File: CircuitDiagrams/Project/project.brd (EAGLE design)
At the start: 100 x 70 mm, 124 parts, among them IC1 UC3C, IC2 PCA9542A, IC3 MT48LC4M16A2TSOP54, IC4 TB6593FNGSSOP20, IC5 TB6593FNGSSOP20, J1 JTAG2.54MM2X5TH, J2 1BY2THROUGHHOLE, J3 1BY2THROUGHHOLE, J4 1BY2THROUGHHOLE, J5 8PIN2.54MM2X4TH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

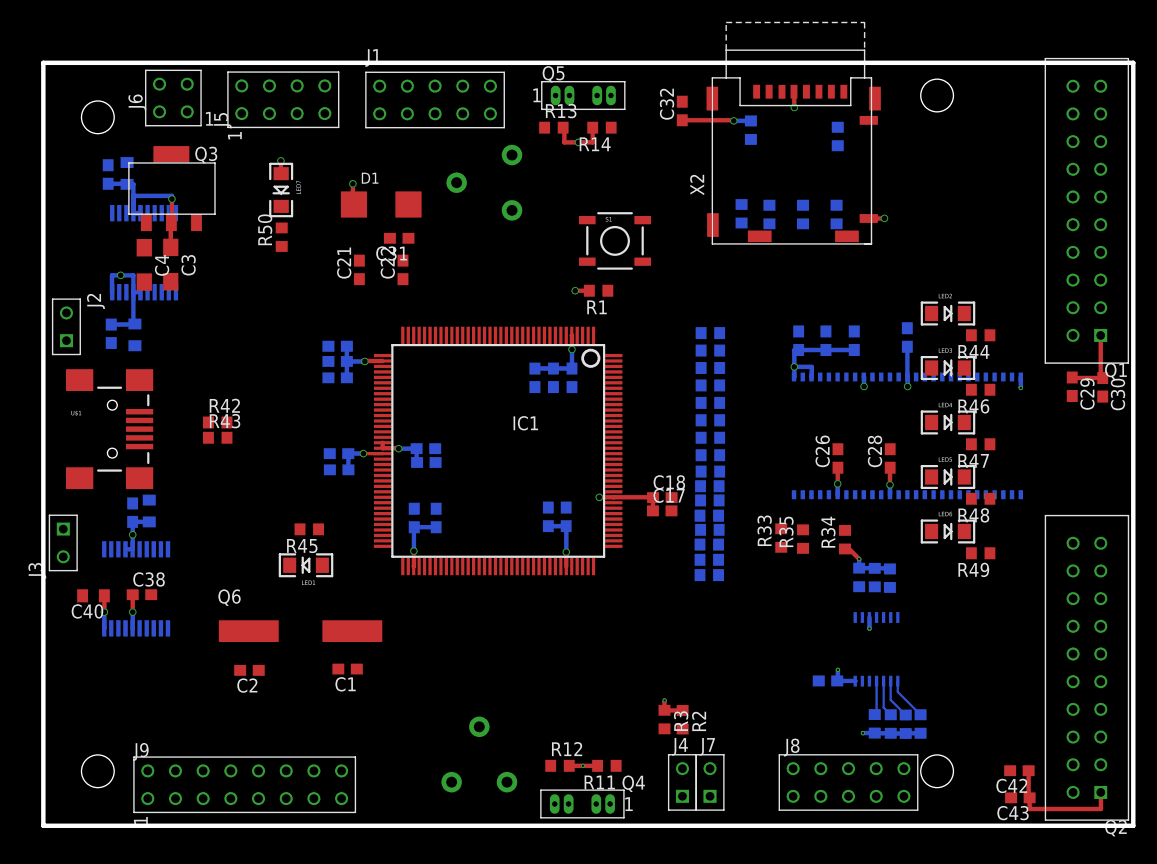
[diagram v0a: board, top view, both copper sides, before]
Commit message: Half way through routing the GND Connections
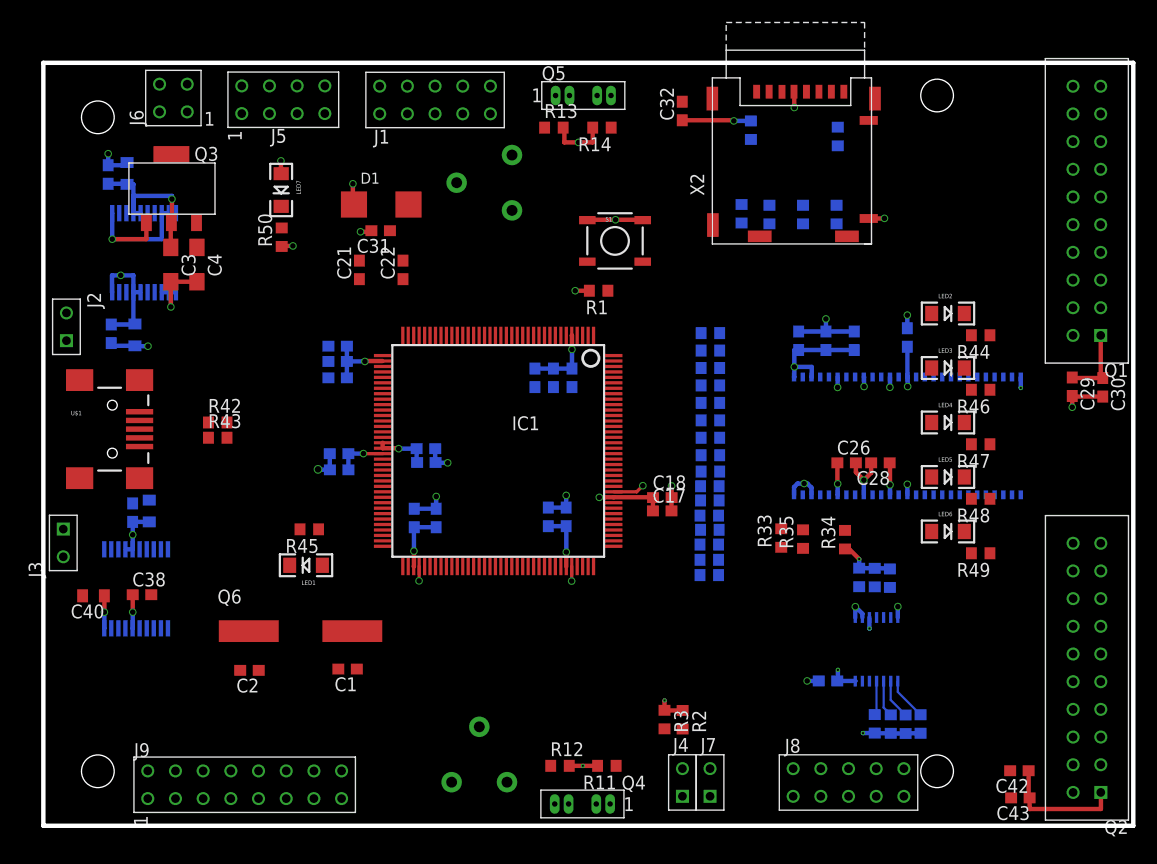
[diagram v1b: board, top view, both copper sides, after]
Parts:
- moved C4 4.83 mm to (14.1, 51.5)
- moved C31 1.84 mm to (30.9, 54.6)
- moved C28 0.98 mm to (76.8, 33.3), turned to 180 degrees
- moved C26 0.89 mm to (73.7, 33.3), turned to 0 degrees
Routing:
- net GND: track 0.00 -> 83.5 mm, vias 0 -> 26

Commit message: Finished Wiring GND. Done USB Data and oscillator
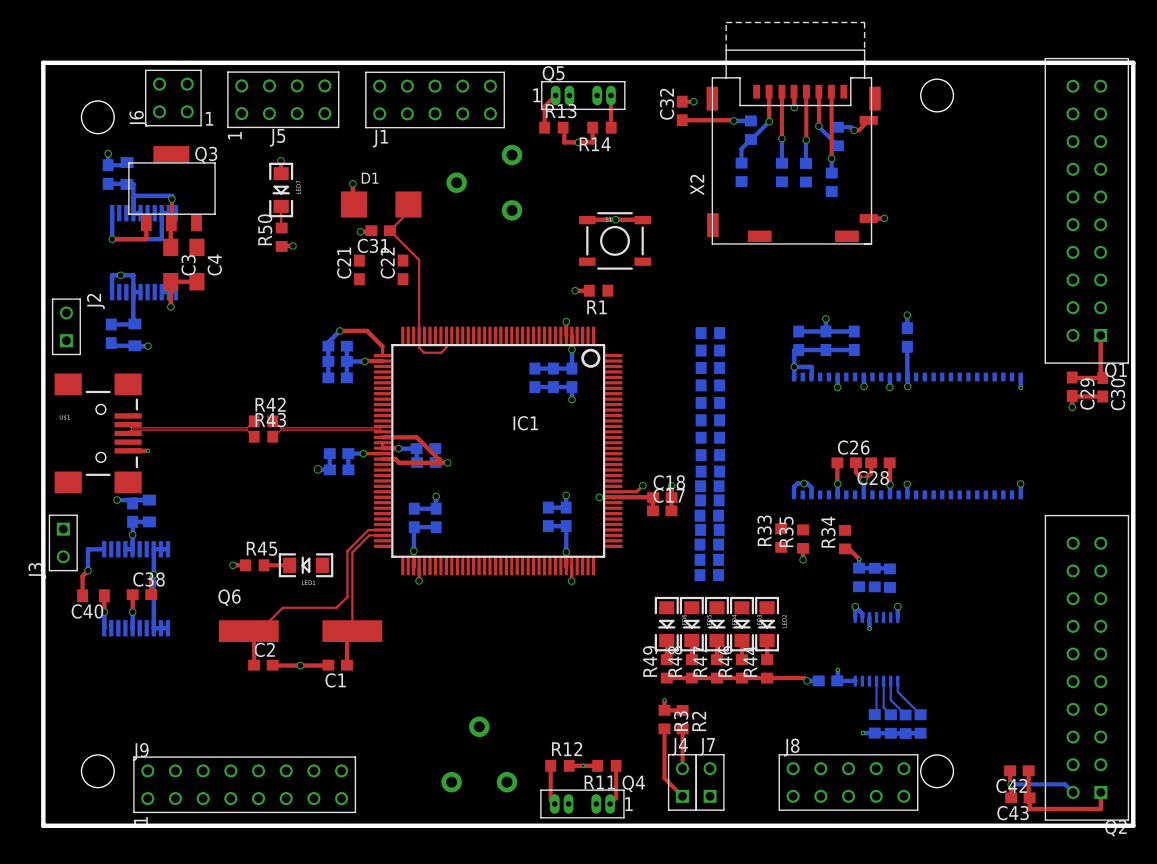
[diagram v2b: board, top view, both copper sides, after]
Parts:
- moved R44 36.3 mm to (66.4, 14.4), turned to 90 degrees
- moved R46 33.7 mm to (64.1, 14.4), turned to 90 degrees
- moved LED2 33.0 mm to (66.4, 18.5), turned to 270 degrees
- moved R47 31.8 mm to (61.8, 14.4), turned to 90 degrees
- moved R48 30.8 mm to (59.5, 14.4), turned to 90 degrees
- moved R49 30.7 mm to (57.2, 14.4), turned to 90 degrees
- moved LED3 30.2 mm to (64.1, 18.5), turned to 270 degrees
- moved LED4 28.1 mm to (61.8, 18.5), turned to 270 degrees
- moved LED6 27.2 mm to (57.2, 18.5), turned to 270 degrees
- moved LED5 27.1 mm to (59.5, 18.5), turned to 270 degrees
- moved R45 5.99 mm to (19.4, 23.9), turned to 0 degrees
- moved R42 4.20 mm to (20.2, 37.1)
- moved R43 4.20 mm to (20.2, 35.7)
- moved R38 4.02 mm to (67.8, 59.9)
- moved R39 3.85 mm to (70.0, 59.9)
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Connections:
- net N$28 renamed DATA_N
- net N$29 renamed DATA_P
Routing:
- net GND: track 83.5 -> 173.3 mm, vias 26 -> 40
- net PB30: track 0.00 -> 21.6 mm
- net PA16: track 0.00 -> 19.0 mm
- net PB31: track 0.00 -> 14.0 mm
- net USB_N: track 0.00 -> 11.9 mm
- net USB_P: track 0.00 -> 11.9 mm
- net DATA_P: track 0.00 -> 10.4 mm
- net DATA_N: track 0.00 -> 10.4 mm
- net N$23: track 0.00 -> 7.64 mm, vias 0 -> 1
- net N$27: track 0.00 -> 7.48 mm, vias 0 -> 1
- net PC2: track 0.00 -> 6.87 mm
- net N$26: track 0.00 -> 6.60 mm, vias 0 -> 1
- net N$25: track 0.00 -> 6.56 mm, vias 0 -> 1
- net N$5: track 0.00 -> 3.73 mm
- net PA6: track 0.00 -> 3.65 mm
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
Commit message: Routed DQ Lines on the SDRAM.
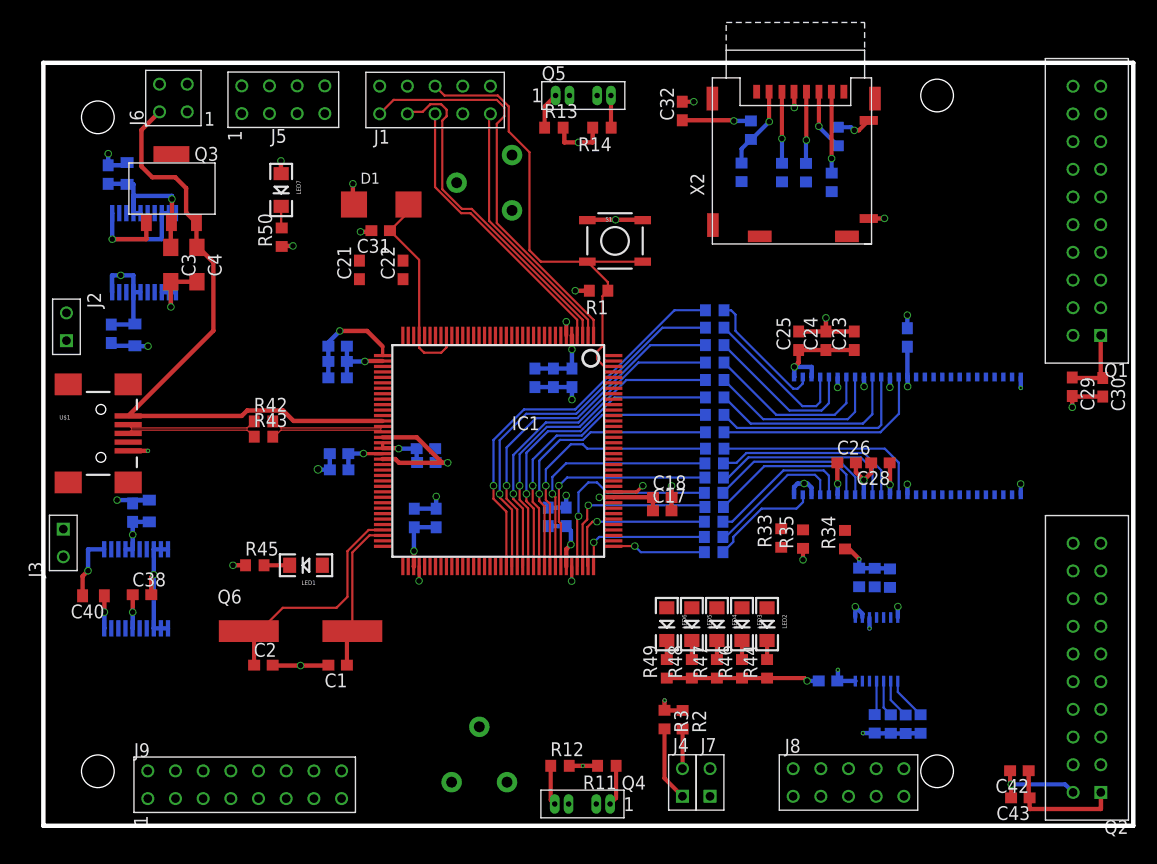
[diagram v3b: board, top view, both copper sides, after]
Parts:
- moved R18 2.14 mm to (61.6, 45.7)
- moved R19 2.14 mm to (61.6, 44.1)
- moved R20 2.14 mm to (61.6, 42.5)
- moved R21 2.14 mm to (61.6, 40.9)
- moved R23 2.14 mm to (61.6, 37.7)
- moved R24 2.14 mm to (61.6, 36.1)
- moved R25 2.14 mm to (61.6, 34.6)
- moved R26 2.14 mm to (61.5, 33.2)
- moved R28 2.14 mm to (61.5, 30.6)
- moved R29 2.14 mm to (61.5, 29.2)
- moved R31 2.14 mm to (61.5, 26.5)
- moved R32 2.14 mm to (61.5, 25.1)
- moved R27 2.14 mm to (61.5, 31.9)
- moved R30 2.14 mm to (61.5, 27.9)
- moved R17 2.14 mm to (61.6, 47.3)
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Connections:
- net N$10 renamed DQ03
- net N$11 renamed DQ04
- net N$12 renamed DQ05
- net N$13 renamed DQ06
- net N$14 renamed DQ07
- net N$15 renamed DQ08
- net N$16 renamed DQ09
- net N$17 renamed DQ10
- net N$18 renamed DQ11
- net N$19 renamed DQ12
- net N$20 renamed DQ13
- net N$21 renamed DQ14
- net N$22 renamed DQ15
- net N$7 renamed DQ00
- net N$8 renamed DQ01
- net N$9 renamed DQ02
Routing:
- net +5V: track 0.00 -> 59.8 mm
- net RESET_N: track 0.00 -> 44.3 mm
- net PA0: track 0.00 -> 37.1 mm
- net PC19: track 0.00 -> 36.5 mm, vias 0 -> 1
- net PC20: track 0.00 -> 35.2 mm, vias 0 -> 1
- net PC21: track 0.00 -> 33.5 mm, vias 0 -> 1
- net PC22: track 0.00 -> 31.7 mm, vias 0 -> 1
- net PA2: track 0.00 -> 30.9 mm
- net PC23: track 0.00 -> 30.5 mm, vias 0 -> 1
- net PC24: track 0.00 -> 29.3 mm, vias 0 -> 1
- net PC25: track 0.00 -> 27.6 mm, vias 0 -> 1
- net PC26: track 0.00 -> 26.2 mm, vias 0 -> 1
- net PA3: track 0.00 -> 26.2 mm
- net PC27: track 0.00 -> 24.8 mm, vias 0 -> 1
- net PA1: track 0.00 -> 24.1 mm
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
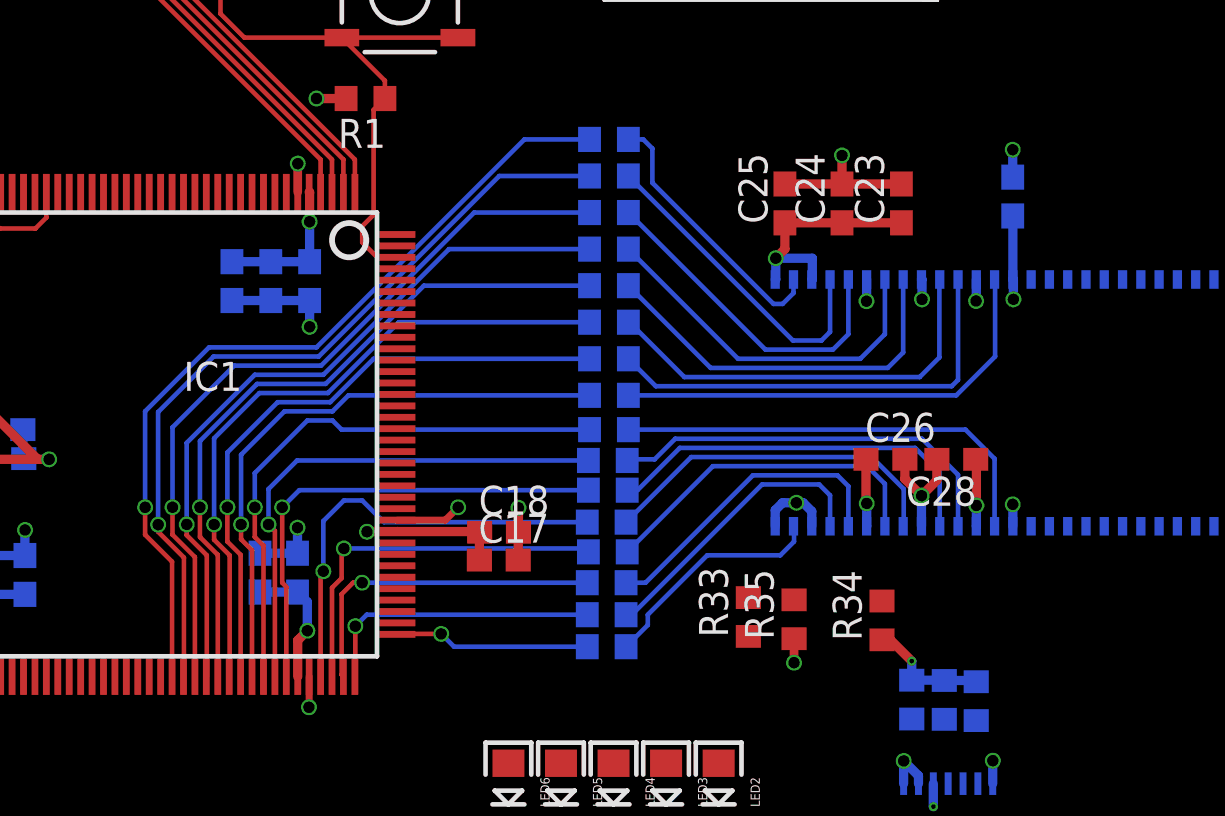
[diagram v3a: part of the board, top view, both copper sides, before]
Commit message: Ripped up SDRAM lines due to poor routing. Working on it again
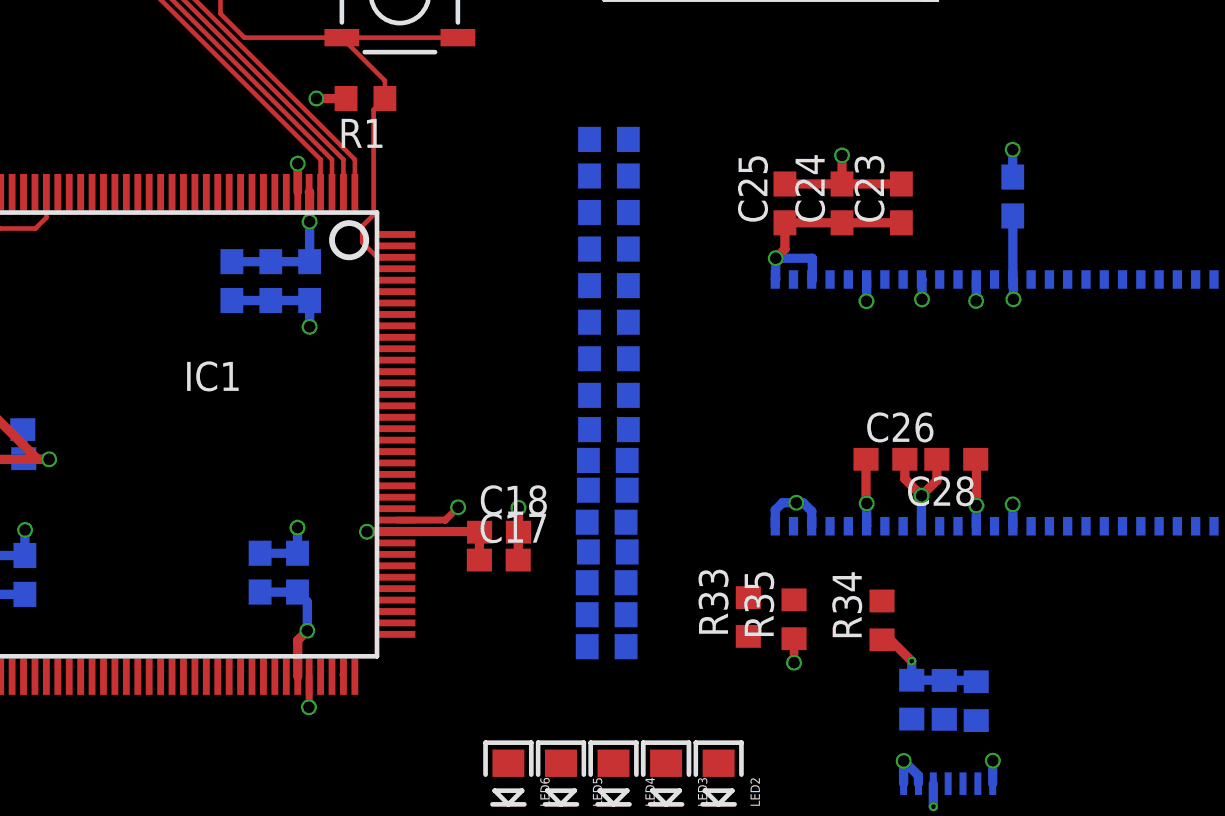
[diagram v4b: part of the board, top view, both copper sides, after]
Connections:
- net N$24 renamed SDRAMCLK
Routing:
- net PC19: track 36.5 -> 0.00 mm, vias 1 -> 0
- net PC20: track 35.2 -> 0.00 mm, vias 1 -> 0
- net PC21: track 33.5 -> 0.00 mm, vias 1 -> 0
- net PC22: track 31.7 -> 0.00 mm, vias 1 -> 0
- net PC23: track 30.5 -> 0.00 mm, vias 1 -> 0
- net PC24: track 29.3 -> 0.00 mm, vias 1 -> 0
- net PC25: track 27.6 -> 0.00 mm, vias 1 -> 0
- net PC26: track 26.2 -> 0.00 mm, vias 1 -> 0
- net PC27: track 24.8 -> 0.00 mm, vias 1 -> 0
- net PC28: track 22.8 -> 0.00 mm, vias 1 -> 0
- net PC29: track 21.2 -> 0.00 mm, vias 1 -> 0
- net DQ07: track 20.1 -> 0.03 mm
- net DQ08: track 19.5 -> 0.00 mm
- net DQ06: track 19.4 -> 0.00 mm
- net PC30: track 19.2 -> 0.00 mm, vias 1 -> 0
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
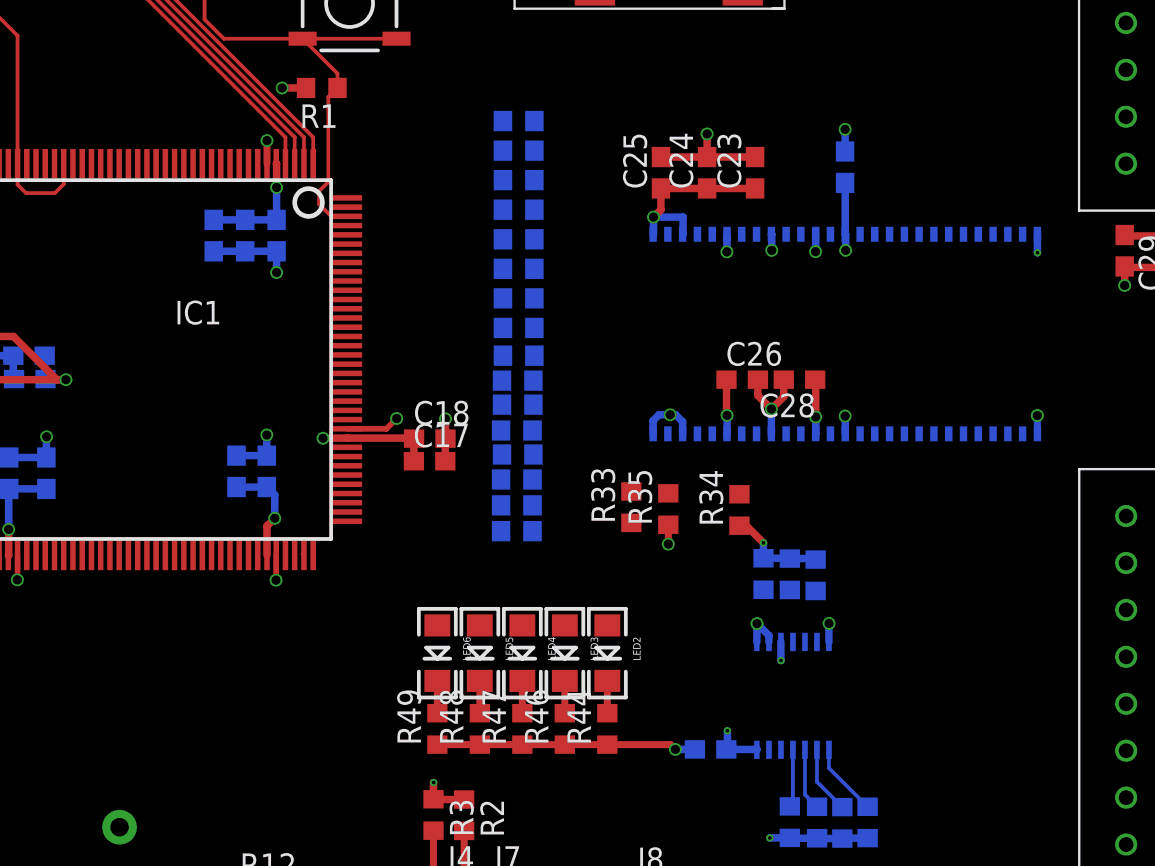
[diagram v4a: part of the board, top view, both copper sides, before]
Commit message: Moved the SRAM to a different place
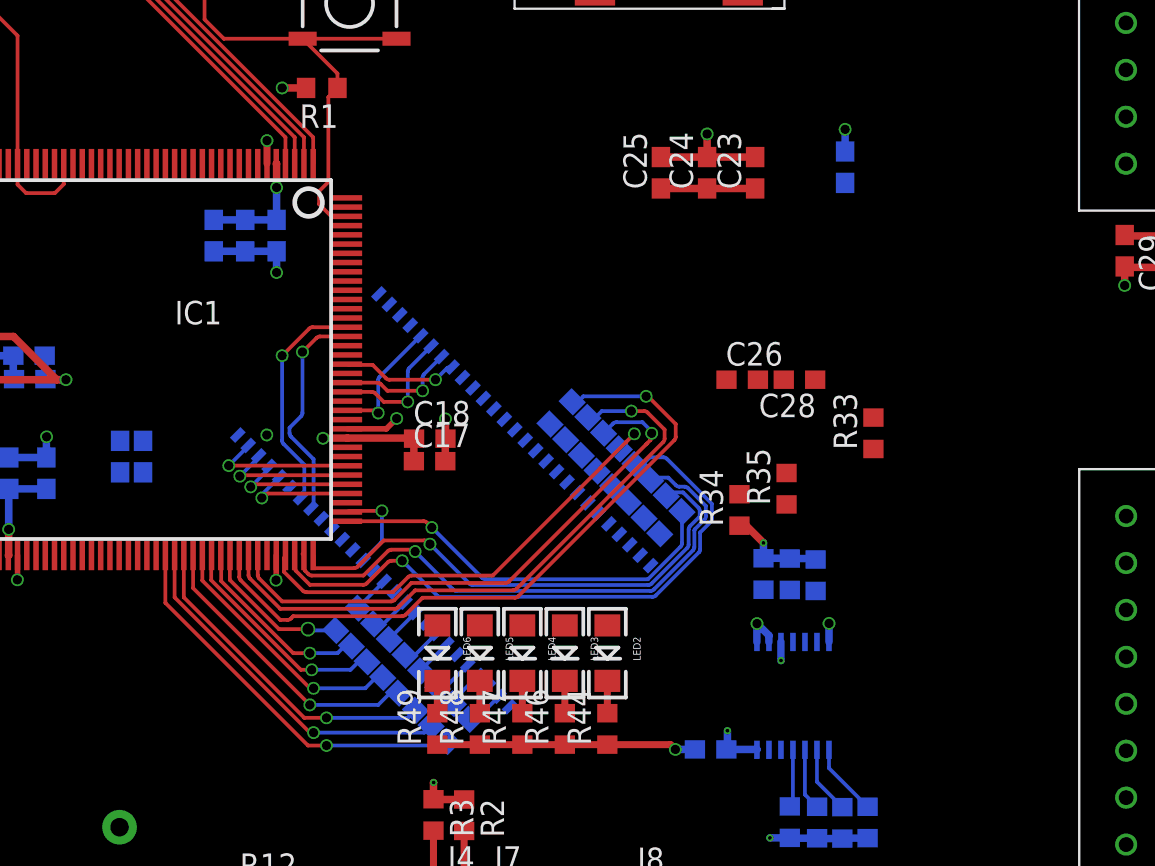
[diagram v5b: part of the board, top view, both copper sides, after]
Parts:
- moved R17 33.1 mm to (58.3, 14.3), turned to 315 degrees
- moved R18 30.8 mm to (57.5, 15.2), turned to 315 degrees
- moved R19 28.5 mm to (56.6, 16.0), turned to 315 degrees
- moved R20 26.2 mm to (55.7, 16.9), turned to 315 degrees
- moved R21 24.1 mm to (54.8, 17.8), turned to 315 degrees
- moved IC3 22.5 mm to (58.1, 26.2), turned to 135 degrees
- moved R22 22.0 mm to (54.0, 18.6), turned to 315 degrees
- moved R23 20.1 mm to (53.2, 19.5), turned to 315 degrees
- moved R24 18.3 mm to (52.3, 20.3), turned to 315 degrees
- moved R33 13.7 mm to (80.8, 30.4)
- moved R32 8.35 mm to (69.8, 25.6), turned to 135 degrees
- moved R31 7.49 mm to (69.0, 26.4), turned to 135 degrees
- moved C16 6.75 mm to (41.3, 29.1)
- moved R30 6.67 mm to (68.1, 27.3), turned to 135 degrees
- moved R35 6.49 mm to (76.1, 27.4)
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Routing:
- net PC27: track 0.00 -> 36.9 mm, vias 0 -> 1
- net PC31: track 0.00 -> 33.7 mm, vias 0 -> 1
- net PC28: track 0.00 -> 33.4 mm, vias 0 -> 1
- net PD0: track 0.11 -> 30.7 mm, vias 0 -> 1
- net PC29: track 0.00 -> 30.0 mm, vias 0 -> 1
- net PD1: track 0.03 -> 28.3 mm, vias 0 -> 1
- net PC30: track 0.00 -> 25.0 mm, vias 0 -> 1
- net PD2: track 0.03 -> 22.0 mm, vias 0 -> 1
- net +3V3: track 154.9 -> 133.0 mm, vias 30 -> 23
- net PC19: track 0.00 -> 21.1 mm, vias 0 -> 1
- net PC20: track 0.00 -> 19.3 mm, vias 0 -> 1
- net PC21: track 0.00 -> 17.7 mm, vias 0 -> 1
- net GND: track 173.5 -> 157.5 mm, vias 40 -> 33
- net PC22: track 0.00 -> 15.8 mm, vias 0 -> 1
- net PC23: track 0.00 -> 13.8 mm, vias 0 -> 1
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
